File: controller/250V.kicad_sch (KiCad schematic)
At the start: 9 parts, among them J1 LRS-100-12, J2 WAGO, J3 WAGO, J4 WAGO, K2 G6DN-1ADC4.5, K3 G6DN-1ADC4.5, P1 IEC_60320_C13_Plug, P2 Lamp1, P3 Lamp2

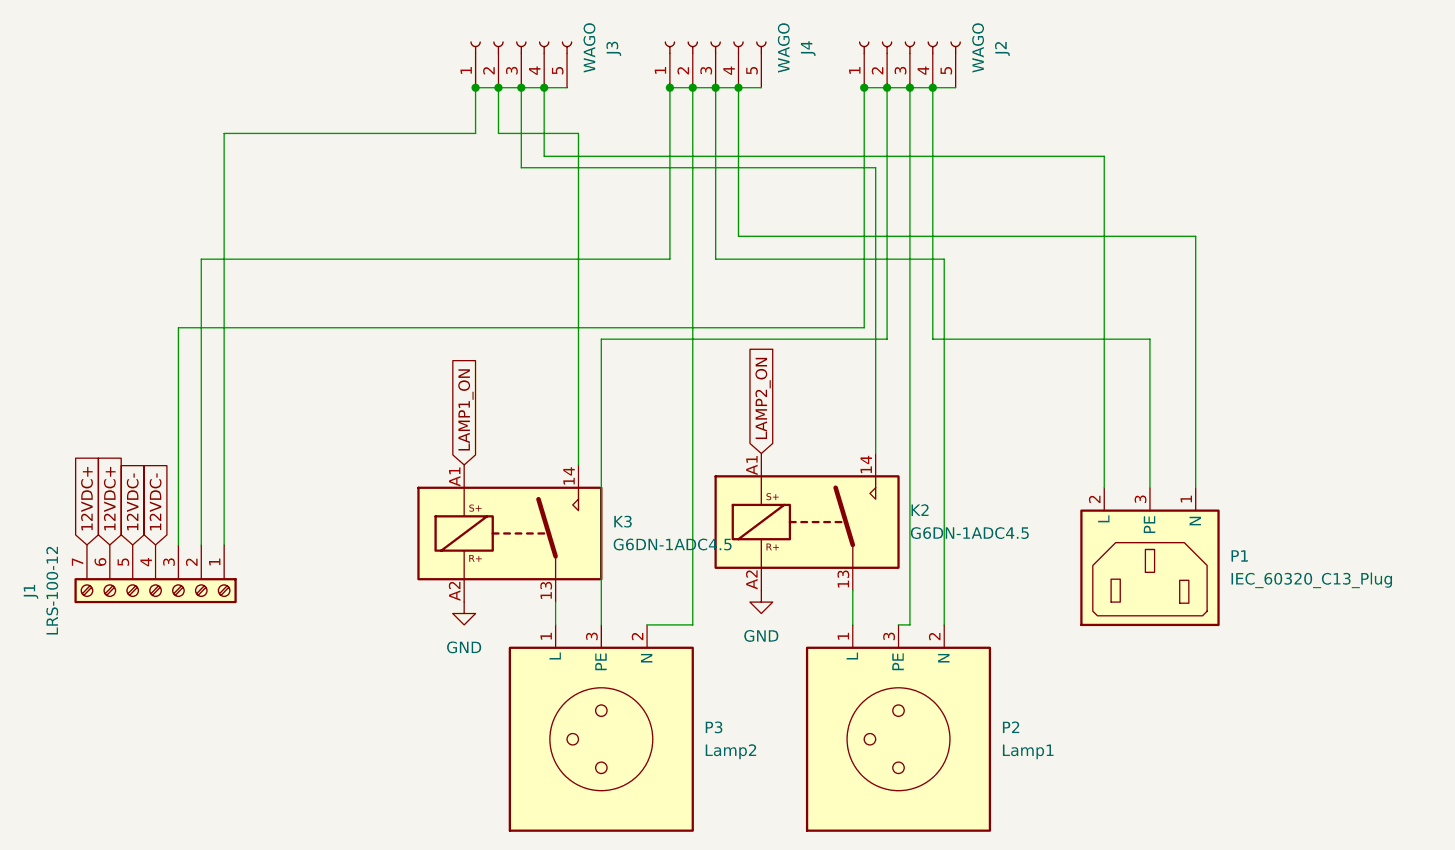
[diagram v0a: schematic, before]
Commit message: updated relays and 250V part with actual circuit
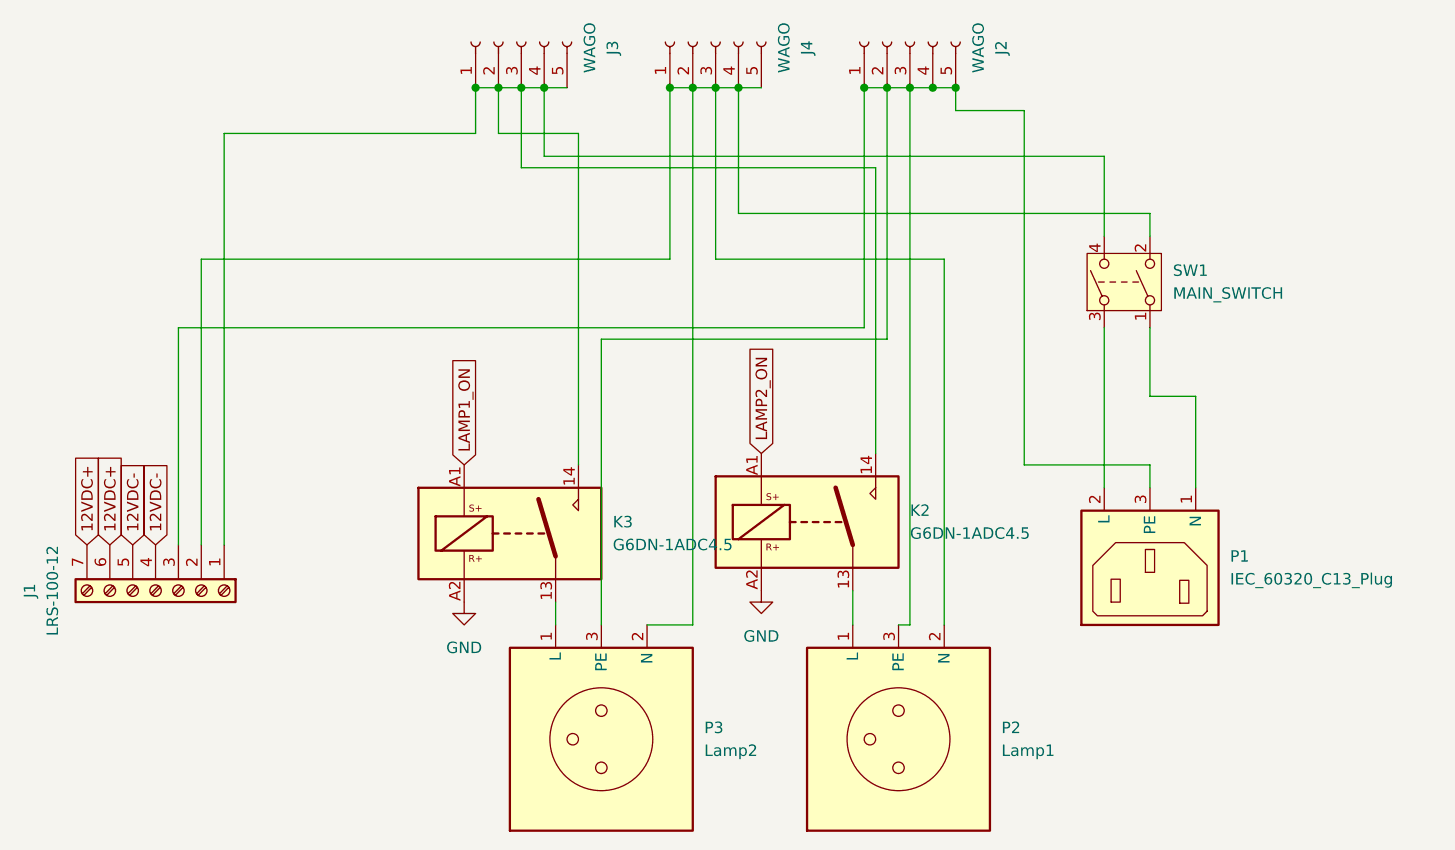
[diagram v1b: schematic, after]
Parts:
- added SW1: MAIN_SWITCH, symbol Switch:SW_DPST
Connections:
- net at J1.1 (Pin_1), J3.1 (Pin_1), J3.2 (Pin_2)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: now also SW1.4; no longer P1.2 (L)
- net at J1.2 (Pin_2), J4.1 (Pin_1), J4.2 (Pin_2)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: now also SW1.2; no longer P1.1 (N)
- new net: P1.1 (N), SW1.1
- new net: P1.2 (L), SW1.3
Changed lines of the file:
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@@
+	)
+	(junction
+		(at 133.35 33.02)
+		(diameter 0)
+		(color 0 0 0 0)
 	)
 	(junction
@@
 	(wire
 		(pts
+			(xy 109.22 46.99) (xy 109.22 33.02)
+		)
+		(stroke
+			(width 0)
+			(type default)
+		)
+	)
+	(wire
+		(pts
+			(xy 160.02 67.31) (xy 160.02 77.47)
+		)
+		(stroke
+			(width 0)
+			(type default)
+		)
+	)
+	(wire
+		(pts
 			(xy 125.73 33.02) (xy 123.19 33.02)
 		)
@@
 	(wire
 		(pts
-			(xy 149.86 77.47) (xy 149.86 40.64)
+			(xy 154.94 67.31) (xy 154.94 59.69)
+		)
+		(stroke
+			(width 0)
+			(type default)
+		)
+	)
+	(wire
+		(pts
+			(xy 149.86 77.47) (xy 149.86 59.69)
 		)
 		(stroke
@@
 	(wire
 		(pts
-			(xy 154.94 60.96) (xy 130.81 60.96)
-		)
-		(stroke
-			(width 0)
-			(type default)
-		)
-	)
-	(wire
-		(pts
-			(xy 109.22 49.53) (xy 109.22 33.02)
+			(xy 154.94 74.93) (xy 140.97 74.93)
 		)
 		(stroke
@@
 	(wire
 		(pts
-			(xy 154.94 77.47) (xy 154.94 60.96)
+			(xy 154.94 74.93) (xy 154.94 77.47)
 		)
 		(stroke
@@
 	(wire
 		(pts
+			(xy 109.22 46.99) (xy 154.94 46.99)
+		)
+		(stroke
+			(width 0)
+			(type default)
+		)
+	)
+	(wire
+		(pts
 			(xy 132.08 52.07) (xy 106.68 52.07)
 		)
@@
 	(wire
 		(pts
-			(xy 160.02 77.47) (xy 160.02 49.53)
+			(xy 140.97 35.56) (xy 133.35 35.56)
 		)
 		(stroke
@@
 	(wire
 		(pts
+			(xy 160.02 67.31) (xy 154.94 67.31)
+		)
+		(stroke
+			(width 0)
+			(type default)
+		)
+	)
+	(wire
+		(pts
+			(xy 133.35 35.56) (xy 133.35 33.02)
+		)
+		(stroke
+			(width 0)
+			(type default)
+		)
+	)
+	(wire
+		(pts
 			(xy 124.46 73.66) (xy 124.46 41.91)
 		)
@@
 	(wire
 		(pts
-			(xy 160.02 49.53) (xy 109.22 49.53)
+			(xy 154.94 49.53) (xy 154.94 46.99)
 		)
 		(stroke
@@
 	(wire
 		(pts
-			(xy 130.81 60.96) (xy 130.81 33.02)
+			(xy 140.97 74.93) (xy 140.97 35.56)
 		)
 		(stroke
@@
 		(pts
 			(xy 87.63 40.64) (xy 87.63 33.02)
+		)
+		(stroke
+			(width 0)
+			(type default)
+		)
+	)
+	(wire
+		(pts
+			(xy 149.86 49.53) (xy 149.86 40.64)
 		)
 		(stroke
@@
 					(unit 1)
 				)
+			)
+		)
+	)
+	(symbol
+		(lib_id "Switch:SW_DPST")
+		(at 152.4 54.61 90)
+		(unit 1)
+		(exclude_from_sim no)
+		(in_bom yes)
+		(on_board yes)
+		(dnp no)
+		(fields_autoplaced yes)
+		(property "Reference" "SW1"
+			(at 157.48 53.3399 90)
+			(effects
+				(font
+					(size 1.27 1.27)
+				)
+				(justify right)
+			)
+		)
+		(property "Value" "MAIN_SWITCH"
+			(at 157.48 55.8799 90)
+			(effects
+				(font
+					(size 1.27 1.27)
+				)
+				(justify right)
+			)
+		)
+		(property "Footprint" ""
+			(at 152.4 54.61 0)
+			(effects
+				(font
+					(size 1.27 1.27)
+				)
+				(hide yes)
+			)
+		)
+		(property "Datasheet" "~"
+			(at 152.4 54.61 0)
+			(effects
+				(font
+					(size 1.27 1.27)
+				)
+				(hide yes)
+			)
+		)
+		(property "Description" "Double Pole Single Throw (DPST) Switch"
+			(at 152.4 54.61 0)
+			(effects
+				(font
+					(size 1.27 1.27)
+				)
+				(hide yes)
+			)
+		)
+		(pin "4"
+		)
+		(pin "1"
+		)
+		(pin "3"
+		)
+		(pin "2"
+		)
+		(instances
+			(project "controller"
+				(path "/6656c305-24d1-4d05-82fa-e34e3bee2322/0328dde9-ba00-42b8-a20a-86a4f018b5ab"
+					(reference "SW1")
+					(unit 1)
+				)
